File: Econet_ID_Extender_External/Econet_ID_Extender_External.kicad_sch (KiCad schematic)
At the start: 3 parts, among them J1 Conn_02x06_Odd_Even, SW1 SW_DIP_x08

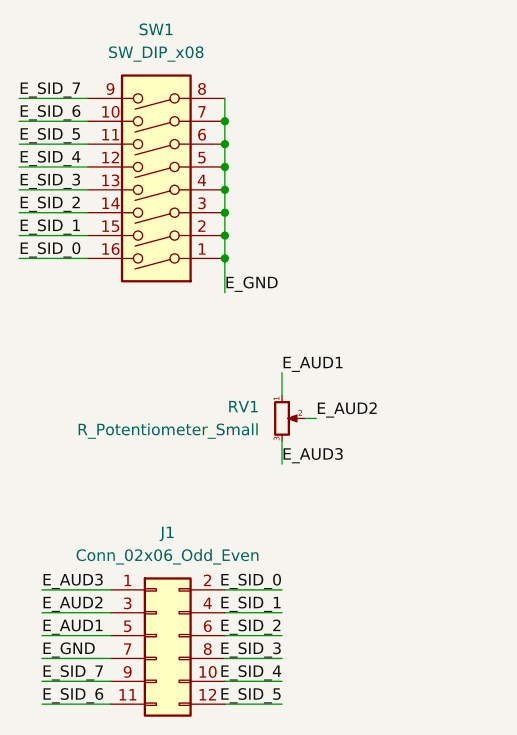
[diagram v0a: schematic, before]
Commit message: Swap to standard 2.54 pitch ribbon
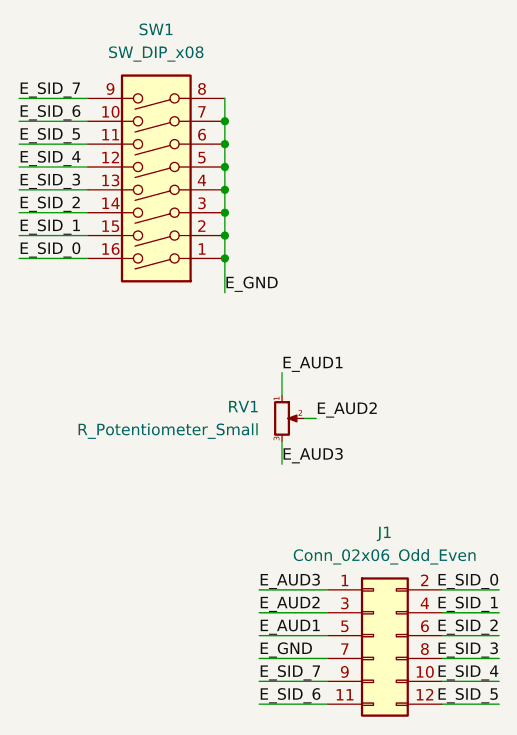
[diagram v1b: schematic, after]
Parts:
- J1: footprint AliExpress_Stuff:MicroMatch-12p-SMD -> Connector_PinHeader_2.54mm:PinHeader_2x06_P2.54mm_Vertical_SMD
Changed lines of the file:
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@@
   (junction (at 147.32 69.85) (diameter 0) (color 0 0 0 0)
   )
-  (wire (pts (xy 147.32 119.38) (xy 153.67 119.38))
+  (wire (pts (xy 171.45 119.38) (xy 177.8 119.38))
+    (stroke (width 0) (type default) (color 0 0 0 0))
+  )
+  (wire (pts (xy 171.45 114.3) (xy 177.8 114.3))
     (stroke (width 0) (type default) (color 0 0 0 0))
   )
@@
     (stroke (width 0) (type default) (color 0 0 0 0))
   )
+  (wire (pts (xy 171.45 124.46) (xy 177.8 124.46))
+    (stroke (width 0) (type default) (color 0 0 0 0))
+  )
   (wire (pts (xy 147.32 77.47) (xy 147.32 81.28))
     (stroke (width 0) (type default) (color 0 0 0 0))
   )
+  (wire (pts (xy 151.13 116.84) (xy 158.75 116.84))
+    (stroke (width 0) (type default) (color 0 0 0 0))
+  )
   (wire (pts (xy 124.46 62.23) (xy 132.08 62.23))
     (stroke (width 0) (type default) (color 0 0 0 0))
   )
+  (wire (pts (xy 171.45 116.84) (xy 177.8 116.84))
+    (stroke (width 0) (type default) (color 0 0 0 0))
+  )
   (wire (pts (xy 153.67 97.79) (xy 153.67 100.33))
     (stroke (width 0) (type default) (color 0 0 0 0))
   )
-  (wire (pts (xy 147.32 124.46) (xy 153.67 124.46))
-    (stroke (width 0) (type default) (color 0 0 0 0))
-  )
-  (wire (pts (xy 147.32 127) (xy 153.67 127))
-    (stroke (width 0) (type default) (color 0 0 0 0))
-  )
   (wire (pts (xy 147.32 64.77) (xy 147.32 67.31))
     (stroke (width 0) (type default) (color 0 0 0 0))
   )
-  (wire (pts (xy 127 127) (xy 134.62 127))
-    (stroke (width 0) (type default) (color 0 0 0 0))
-  )
   (wire (pts (xy 124.46 69.85) (xy 132.08 69.85))
     (stroke (width 0) (type default) (color 0 0 0 0))
@@
     (stroke (width 0) (type default) (color 0 0 0 0))
   )
-  (wire (pts (xy 147.32 114.3) (xy 153.67 114.3))
-    (stroke (width 0) (type default) (color 0 0 0 0))
-  )
   (wire (pts (xy 147.32 72.39) (xy 147.32 74.93))
     (stroke (width 0) (type default) (color 0 0 0 0))
   )
-  (wire (pts (xy 127 121.92) (xy 134.62 121.92))
-    (stroke (width 0) (type default) (color 0 0 0 0))
-  )
-  (wire (pts (xy 127 116.84) (xy 134.62 116.84))
-    (stroke (width 0) (type default) (color 0 0 0 0))
-  )
   (wire (pts (xy 147.32 62.23) (xy 147.32 64.77))
     (stroke (width 0) (type default) (color 0 0 0 0))
   )
-  (wire (pts (xy 127 124.46) (xy 134.62 124.46))
+  (wire (pts (xy 151.13 114.3) (xy 158.75 114.3))
+    (stroke (width 0) (type default) (color 0 0 0 0))
+  )
+  (wire (pts (xy 171.45 127) (xy 177.8 127))
     (stroke (width 0) (type default) (color 0 0 0 0))
   )
@@
     (stroke (width 0) (type default) (color 0 0 0 0))
   )
-  (wire (pts (xy 147.32 121.92) (xy 153.67 121.92))
-    (stroke (width 0) (type default) (color 0 0 0 0))
-  )
-  (wire (pts (xy 147.32 116.84) (xy 153.67 116.84))
+  (wire (pts (xy 151.13 124.46) (xy 158.75 124.46))
+    (stroke (width 0) (type default) (color 0 0 0 0))
+  )
+  (wire (pts (xy 151.13 121.92) (xy 158.75 121.92))
+    (stroke (width 0) (type default) (color 0 0 0 0))
+  )
+  (wire (pts (xy 151.13 119.38) (xy 158.75 119.38))
     (stroke (width 0) (type default) (color 0 0 0 0))
   )
@@
     (stroke (width 0) (type default) (color 0 0 0 0))
   )
-  (wire (pts (xy 127 119.38) (xy 134.62 119.38))
-    (stroke (width 0) (type default) (color 0 0 0 0))
-  )
   (wire (pts (xy 124.46 77.47) (xy 132.08 77.47))
     (stroke (width 0) (type default) (color 0 0 0 0))
@@
     (stroke (width 0) (type default) (color 0 0 0 0))
   )
+  (wire (pts (xy 171.45 121.92) (xy 177.8 121.92))
+    (stroke (width 0) (type default) (color 0 0 0 0))
+  )
   (wire (pts (xy 147.32 67.31) (xy 147.32 69.85))
     (stroke (width 0) (type default) (color 0 0 0 0))
   )
-  (wire (pts (xy 127 114.3) (xy 134.62 114.3))
+  (wire (pts (xy 151.13 127) (xy 158.75 127))
     (stroke (width 0) (type default) (color 0 0 0 0))
   )
@@
     (effects (font (size 1.27 1.27)) (justify left bottom))
   )
-  (label "E_SID_2" (at 153.67 119.38 180)
+  (label "E_AUD1" (at 151.13 119.38 0)
+    (effects (font (size 1.27 1.27)) (justify left bottom))
+  )
+  (label "E_SID_2" (at 177.8 119.38 180)
     (effects (font (size 1.27 1.27)) (justify right bottom))
   )
@@
     (effects (font (size 1.27 1.27)) (justify left bottom))
   )
+  (label "E_SID_3" (at 177.8 121.92 180)
+    (effects (font (size 1.27 1.27)) (justify right bottom))
+  )
   (label "E_SID_4" (at 124.46 67.31 0)
     (effects (font (size 1.27 1.27)) (justify left bottom))
@@
     (effects (font (size 1.27 1.27)) (justify left bottom))
   )
-  (label "E_SID_4" (at 153.67 124.46 180)
-    (effects (font (size 1.27 1.27)) (justify right bottom))
+  (label "E_SID_6" (at 151.13 127 0)
+    (effects (font (size 1.27 1.27)) (justify left bottom))
   )
   (label "E_AUD2" (at 157.48 95.25 0)
@@
     (effects (font (size 1.27 1.27)) (justify left bottom))
   )
-  (label "E_GND" (at 127 121.92 0)
-    (effects (font (size 1.27 1.27)) (justify left bottom))
-  )
-  (label "E_SID_7" (at 127 124.46 0)
-    (effects (font (size 1.27 1.27)) (justify left bottom))
-  )
-  (label "E_SID_1" (at 153.67 116.84 180)
-    (effects (font (size 1.27 1.27)) (justify right bottom))
-  )
-  (label "E_SID_5" (at 153.67 127 180)
-    (effects (font (size 1.27 1.27)) (justify right bottom))
-  )
-  (label "E_AUD3" (at 127 114.3 0)
-    (effects (font (size 1.27 1.27)) (justify left bottom))
+  (label "E_SID_7" (at 151.13 124.46 0)
+    (effects (font (size 1.27 1.27)) (justify left bottom))
+  )
+  (label "E_SID_5" (at 177.8 127 180)
+    (effects (font (size 1.27 1.27)) (justify right bottom))
+  )
+  (label "E_SID_1" (at 177.8 116.84 180)
+    (effects (font (size 1.27 1.27)) (justify right bottom))
+  )
+  (label "E_SID_4" (at 177.8 124.46 180)
+    (effects (font (size 1.27 1.27)) (justify right bottom))
   )
   (label "E_AUD1" (at 153.67 90.17 0)
     (effects (font (size 1.27 1.27)) (justify left bottom))
   )
-  (label "E_SID_0" (at 153.67 114.3 180)
-    (effects (font (size 1.27 1.27)) (justify right bottom))
-  )
-  (label "E_AUD2" (at 127 116.84 0)
-    (effects (font (size 1.27 1.27)) (justify left bottom))
-  )
-  (label "E_AUD1" (at 127 119.38 0)
+  (label "E_GND" (at 151.13 121.92 0)
+    (effects (font (size 1.27 1.27)) (justify left bottom))
+  )
+  (label "E_AUD3" (at 151.13 114.3 0)
     (effects (font (size 1.27 1.27)) (justify left bottom))
   )
@@
     (effects (font (size 1.27 1.27)) (justify left bottom))
   )
-  (label "E_SID_6" (at 127 127 0)
-    (effects (font (size 1.27 1.27)) (justify left bottom))
-  )
-  (label "E_SID_3" (at 153.67 121.92 180)
+  (label "E_AUD2" (at 151.13 116.84 0)
+    (effects (font (size 1.27 1.27)) (justify left bottom))
+  )
+  (label "E_SID_0" (at 177.8 114.3 180)
     (effects (font (size 1.27 1.27)) (justify right bottom))
   )
   (label "E_SID_5" (at 124.46 64.77 0)
     (effects (font (size 1.27 1.27)) (justify left bottom))
-  )
-  (symbol (lib_id "Connector_Generic:Conn_02x06_Odd_Even") (at 139.7 119.38 0) (unit 1)
-    (in_bom yes) (on_board yes) (fields_autoplaced)
-    (property "Reference" "J1" (id 0) (at 140.97 107.95 0))
-    (property "Value" "Conn_02x06_Odd_Even" (id 1) (at 140.97 110.49 0))
-    (property "Footprint" "AliExpress_Stuff:MicroMatch-12p-SMD" (id 2) (at 139.7 119.38 0)
-      (effects (font (size 1.27 1.27)) hide)
-    )
-    (property "Datasheet" "~" (id 3) (at 139.7 119.38 0)
-      (effects (font (size 1.27 1.27)) hide)
-    )
-    (pin "1")
-    (pin "10")
-    (pin "11")
-    (pin "12")
-    (pin "2")
-    (pin "3")
-    (pin "4")
-    (pin "5")
-    (pin "6")
-    (pin "7")
-    (pin "8")
-    (pin "9")
   )
   (symbol (lib_id "Switch:SW_DIP_x08") (at 139.7 67.31 180) (unit 1)
@@
     (pin "3")
   )
+  (symbol (lib_id "Connector_Generic:Conn_02x06_Odd_Even") (at 163.83 119.38 0) (unit 1)
+    (in_bom yes) (on_board yes) (fields_autoplaced)
+    (property "Reference" "J1" (id 0) (at 165.1 107.95 0))
+    (property "Value" "Conn_02x06_Odd_Even" (id 1) (at 165.1 110.49 0))
+    (property "Footprint" "Connector_PinHeader_2.54mm:PinHeader_2x06_P2.54mm_Vertical_SMD" (id 2) (at 163.83 119.38 0)
+      (effects (font (size 1.27 1.27)) hide)
+    )
+    (property "Datasheet" "~" (id 3) (at 163.83 119.38 0)
+      (effects (font (size 1.27 1.27)) hide)
+    )
+    (pin "1")
+    (pin "10")
+    (pin "11")
+    (pin "12")
+    (pin "2")
+    (pin "3")
+    (pin "4")
+    (pin "5")
+    (pin "6")
+    (pin "7")
+    (pin "8")
+    (pin "9")
+  )
   (sheet_instances
     (path "/" (page "1"))
   )
   (symbol_instances
-    (path "/0ae6d658-2afe-4d84-99ca-036bd96486ca"
-      (reference "J1") (unit 1) (value "Conn_02x06_Odd_Even") (footprint "AliExpress_Stuff:MicroMatch-12p-SMD")
+    (path "/f92354eb-51b1-4cdb-b4a2-07e018478411"
+      (reference "J1") (unit 1) (value "Conn_02x06_Odd_Even") (footprint "Connector_PinHeader_2.54mm:PinHeader_2x06_P2.54mm_Vertical_SMD")
     )
     (path "/aede13de-acd8-4d74-b1b9-f0931b49685c"

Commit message: Fix volume pot orientation
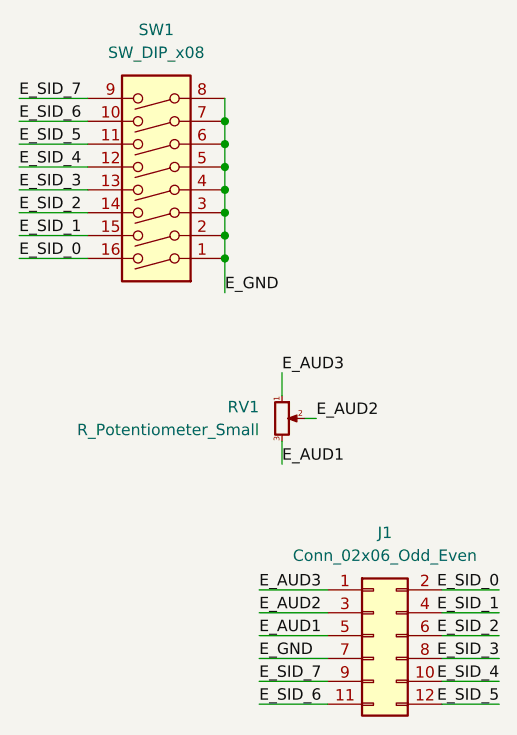
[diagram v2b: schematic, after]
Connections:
- net E_AUD1: now also RV1.3; no longer RV1.1
- net E_AUD3: now also RV1.1; no longer RV1.3
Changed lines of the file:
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@@
     (stroke (width 0) (type default) (color 0 0 0 0))
   )
-  (label "E_AUD3" (at 153.67 100.33 0)
+  (label "E_AUD3" (at 153.67 90.17 0)
     (effects (font (size 1.27 1.27)) (justify left bottom))
   )
@@
     (effects (font (size 1.27 1.27)) (justify right bottom))
   )
-  (label "E_AUD1" (at 153.67 90.17 0)
+  (label "E_AUD1" (at 153.67 100.33 0)
     (effects (font (size 1.27 1.27)) (justify left bottom))
   )
